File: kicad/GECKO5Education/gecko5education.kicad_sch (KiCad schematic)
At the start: 0 parts

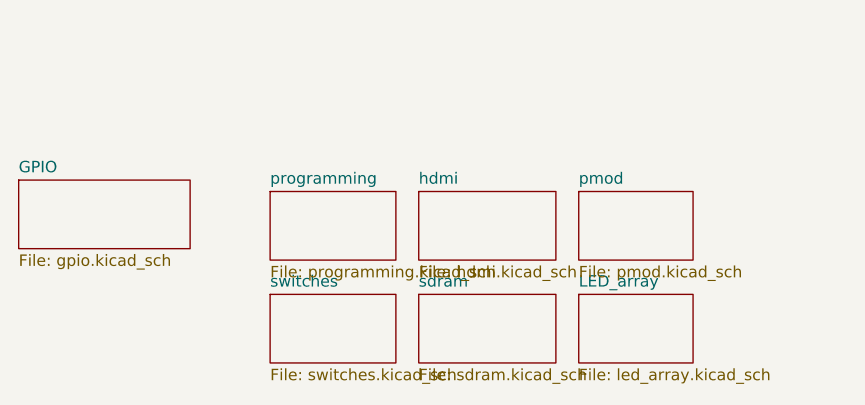
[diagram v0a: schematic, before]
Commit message: Merged perif-add-on to GECKO5
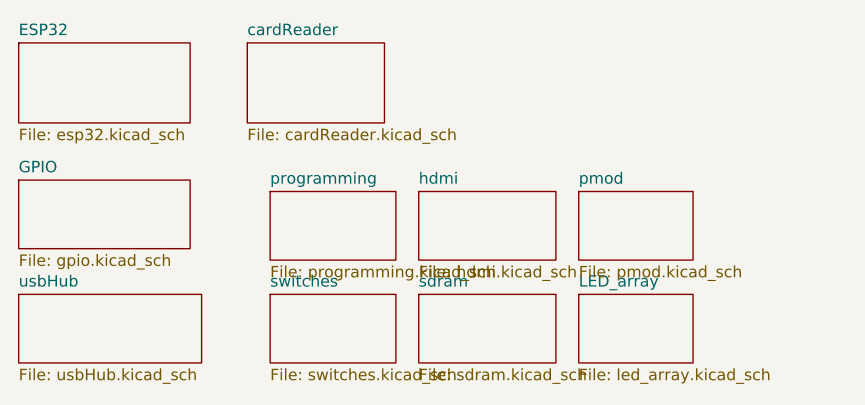
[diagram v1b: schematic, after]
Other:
- added sheet ESP32 (esp32.kicad_sch)
- added sheet cardReader (cardReader.kicad_sch)
- added sheet usbHub (usbHub.kicad_sch)
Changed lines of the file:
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@@
+    )
+  )
+  (sheet (at 185.42 118.11) (size 15.24 8.89) (fields_autoplaced)
+    (stroke (width 0.1524) (type solid))
+    (fill (color 0 0 0 0.0000))
+    (property "Sheetname" "cardReader" (at 185.42 117.3984 0)
+      (effects (font (size 1.27 1.27)) (justify left bottom))
+    )
+    (property "Sheetfile" "cardReader.kicad_sch" (at 185.42 127.5846 0)
+      (effects (font (size 1.27 1.27)) (justify left top))
+    )
+    (instances
+      (project "gecko5education"
+        (path "/47d58937-9286-45a8-b88f-d3fcc6f916c8" (page "11"))
+      )
     )
   )
@@
     )
   )
+  (sheet (at 160.02 118.11) (size 19.05 8.89) (fields_autoplaced)
+    (stroke (width 0.1524) (type solid))
+    (fill (color 0 0 0 0.0000))
+    (property "Sheetname" "ESP32" (at 160.02 117.3984 0)
+      (effects (font (size 1.27 1.27)) (justify left bottom))
+    )
+    (property "Sheetfile" "esp32.kicad_sch" (at 160.02 127.5846 0)
+      (effects (font (size 1.27 1.27)) (justify left top))
+    )
+    (instances
+      (project "gecko5education"
+        (path "/47d58937-9286-45a8-b88f-d3fcc6f916c8" (page "10"))
+      )
+    )
+  )
   (sheet (at 222.25 146.05) (size 12.7 7.62) (fields_autoplaced)
     (stroke (width 0.1524) (type solid))
@@
       )
     )
+  )
+  (sheet (at 160.02 146.05) (size 20.32 7.62) (fields_autoplaced)
+    (stroke (width 0.1524) (type solid))
+    (fill (color 0 0 0 0.0000))
+    (property "Sheetname" "usbHub" (at 160.02 145.3384 0)
+      (effects (font (size 1.27 1.27)) (justify left bottom))
+    )
+    (property "Sheetfile" "usbHub.kicad_sch" (at 160.02 154.2546 0)
+      (effects (font (size 1.27 1.27)) (justify left top))
+    )
+    (instances
+      (project "gecko5education"
+        (path "/47d58937-9286-45a8-b88f-d3fcc6f916c8" (page "9"))
+      )
+    )
